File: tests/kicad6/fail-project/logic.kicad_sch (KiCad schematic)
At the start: 5 parts, among them U1 74LS04

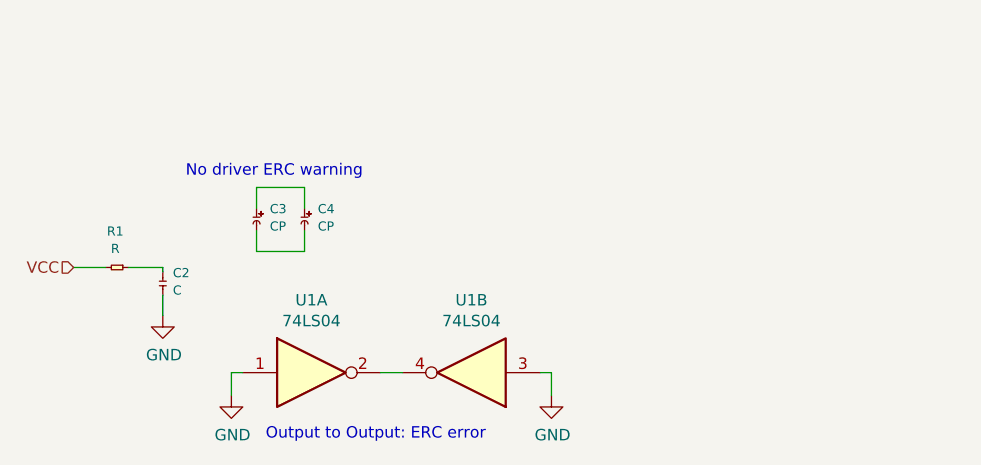
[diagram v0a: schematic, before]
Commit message: Changed the "fail" schematic for v6.
KiCad 6 doesn't report the not drived as a warning.
Now I'm using another warning situation.
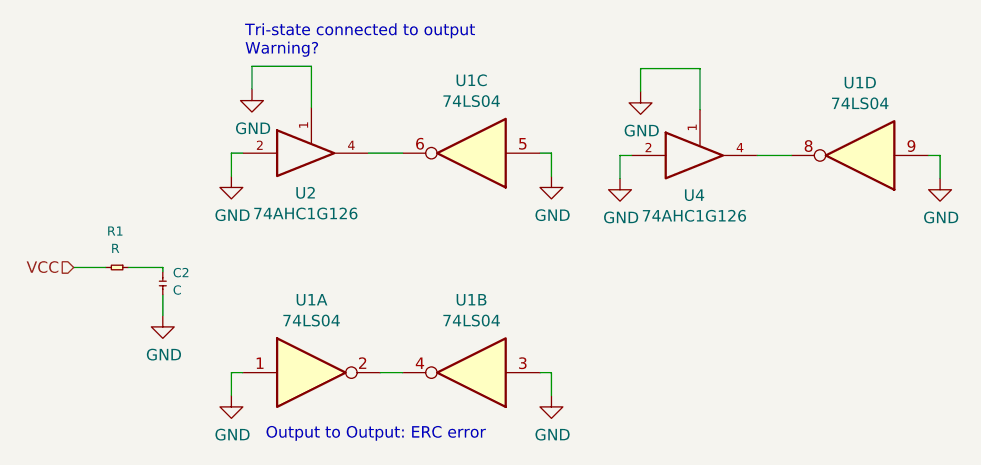
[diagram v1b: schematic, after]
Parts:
- removed C3, C4: CP, Capacitor_SMD:CP_Elec_3x5.3, symbol fail-project-rescue:CP-passive
- added unit 3 of U1
- added unit 4 of U1
- added U2, U4: 74AHC1G126, symbol 74xGxx:74AHC1G126
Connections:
- net GND: now also U1.5, U1.9, U2.1, U2.2, U2.3 (GND), U4.1, U4.2, U4.3 (GND)
- net VCC: now also U2.5 (VCC), U4.5 (VCC)
- new net: U1.6, U2.4
- new net: U1.8, U4.4
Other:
- note added: "Tri-state connected to output Warning?"
- note removed: "No driver ERC warning"
